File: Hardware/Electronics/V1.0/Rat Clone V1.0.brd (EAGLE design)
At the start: 58.5 x 60 mm, 46 parts, among them IC1 LM308, Q1 2N5458

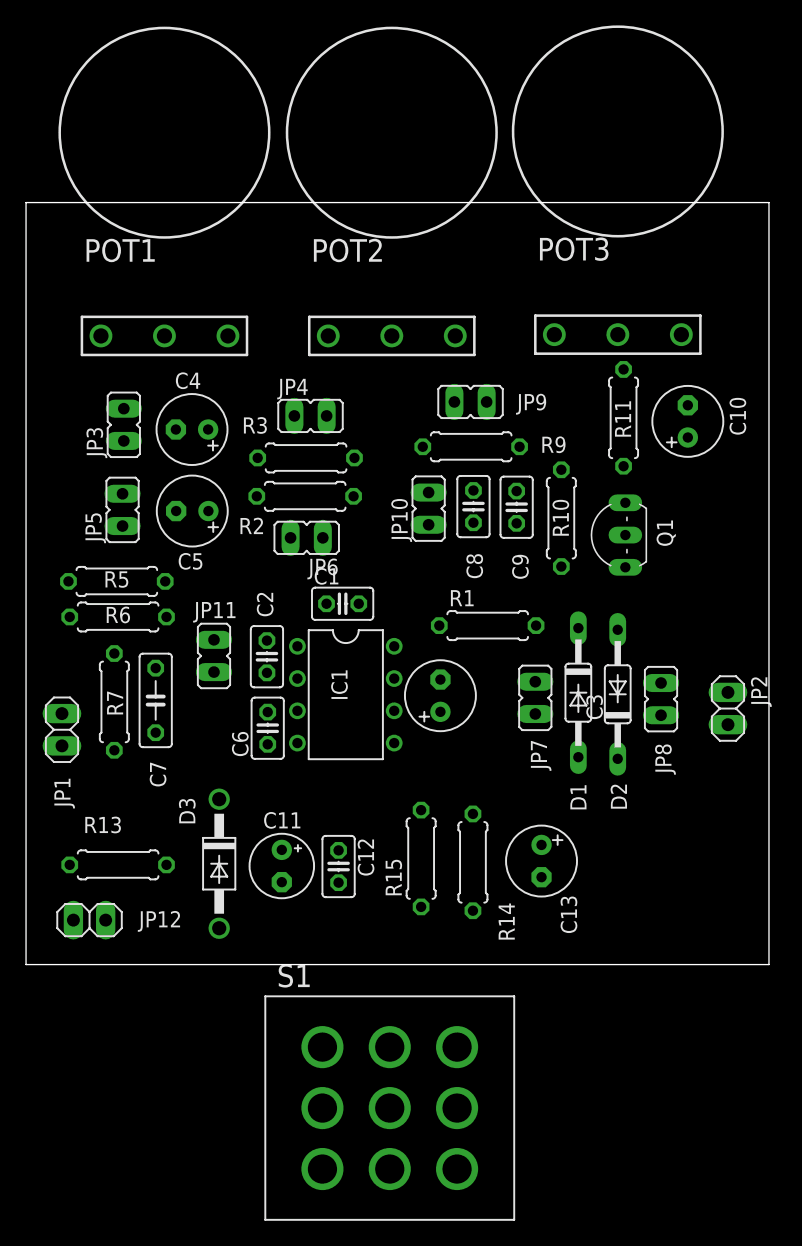
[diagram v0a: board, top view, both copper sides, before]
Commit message: Moved to screw mounted PCB
Basic routing
2 layer same price as 1 layer
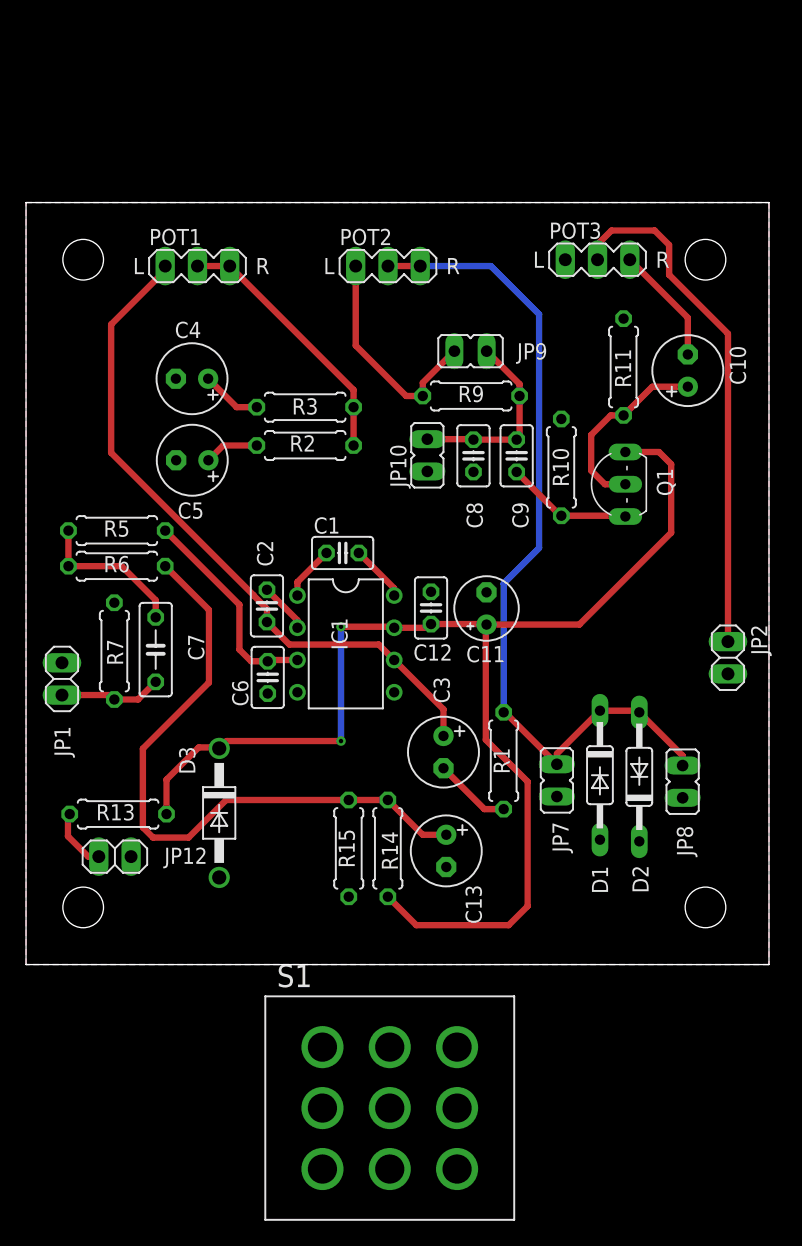
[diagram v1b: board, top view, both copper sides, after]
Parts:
- removed JP11, JP3, JP4, JP5, JP6: (no value), jumper:JP1
- POT1, POT2, POT3: value RV16AF-41-17K-A100K-3 -> 100K; device Custom_Pots:RV16AF-41 -> Custom_Pots:MA03-1
- moved C11 25.9 mm to (36.3, 28.0), turned to 90 degrees
- moved C12 21.6 mm to (31.9, 28.1), turned to 90 degrees
- moved POT1 10.8 mm to (13.5, 55.0)
- moved R1 10.7 mm to (37.6, 16.1), turned to 90 degrees
- moved POT2 10.5 mm to (28.5, 55.0)
- moved POT3 10.2 mm to (45.0, 55.5)
- moved C13 7.54 mm to (33.1, 8.95)
- moved R14 6.79 mm to (28.5, 9.15)
- moved D2 6.72 mm to (48.3, 14.8)
- moved D1 6.72 mm to (45.2, 14.9)
- moved JP7 6.72 mm to (41.8, 14.5)
- moved JP8 6.72 mm to (51.7, 14.4)
- moved R15 5.76 mm to (25.4, 9.15)
- moved JP12 5.39 mm to (7.00, 8.50)
- moved C3 4.45 mm to (32.9, 16.7), turned to 270 degrees
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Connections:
- net GND: now also POT3.L; no longer JP3.1, JP5.2, POT3.1
- net N$10: no longer JP5.1, JP6.2
- net N$11: now also POT2.L; no longer POT2.1
- net N$17: now also POT3.R; no longer POT3.3
- net N$18: now also POT3.M; no longer POT3.2
- net N$21: no longer JP3.2, JP4.1
- net N$4: now also POT1.L; no longer JP11.2, POT1.1
- net N$5: no longer JP11.1
- net N$6: now also POT2.M, POT2.R; no longer POT2.2, POT2.3
- net N$7: now also POT1.M, POT1.R; no longer JP4.2, JP6.1, POT1.2, POT1.3
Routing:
- net +9V: track 0.00 -> 101.5 mm, vias 0 -> 2
- net N$6: track 0.00 -> 66.2 mm
- net N$4: track 0.00 -> 53.7 mm
- net +4V5: track 0.00 -> 50.7 mm
- net N$18: track 0.00 -> 41.0 mm
- net N$7: track 0.00 -> 20.7 mm
- net N$11: track 0.00 -> 17.7 mm
- net N$12: track 0.00 -> 16.8 mm
- net N$15: track 0.00 -> 15.2 mm
- net N$9: track 0.00 -> 15.1 mm
- net N$13: track 0.00 -> 12.1 mm
- net N$16: track 0.00 -> 10.0 mm
- net N$17: track 0.00 -> 9.35 mm
- net N$14: track 0.00 -> 8.10 mm
- net N$3: track 0.00 -> 6.07 mm
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- added copper zone on layer 1, net GND
- added copper zone on layer 16, net GND
